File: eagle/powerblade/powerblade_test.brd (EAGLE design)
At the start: 123 x 88 mm, 107 parts, among them J1 JTAG_14PIN_IDC-NL, J21 AC_INFILM, Q1 2N7002, U1 TPS62122, U2 TR1000, U3 MSP430FR5738, U4 LTC5800, U5 MAX9910, U6 MAX9910, X1 ABM8G, X2 ABS07, Y1 UREACH_XTEND, Y2 ANT-916

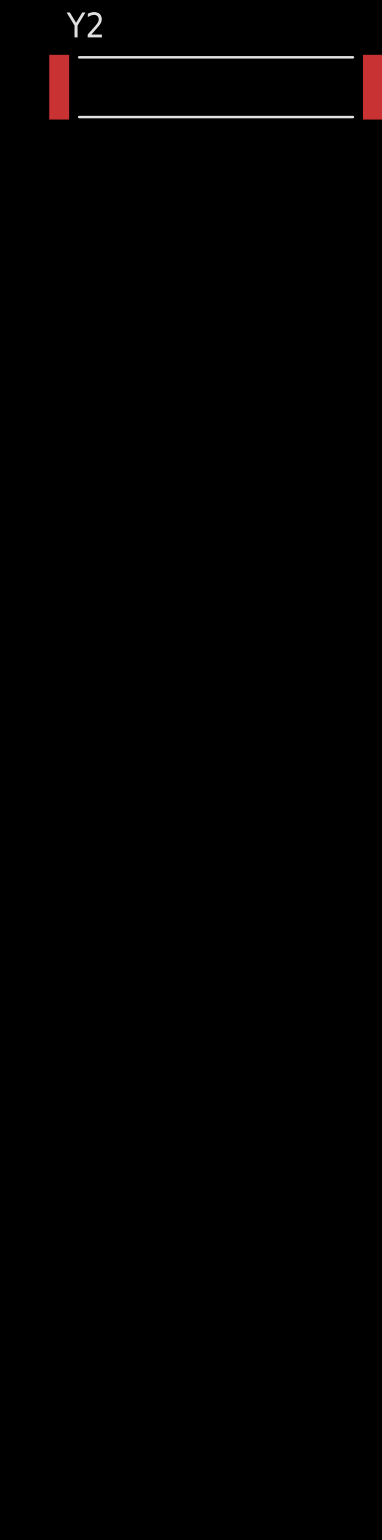
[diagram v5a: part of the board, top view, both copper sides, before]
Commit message: finished final amplifier design including high pass filter and pots for adjusting
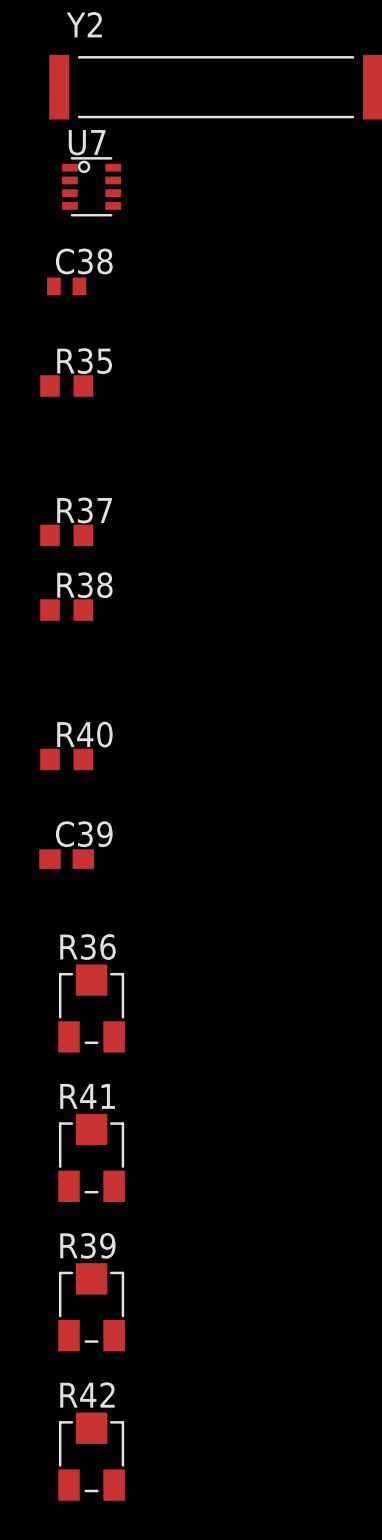
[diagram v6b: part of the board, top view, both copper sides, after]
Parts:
- added C38: 0.1uF, rcl:C0402
- added C39: 1.5uF, rcl:C0603
- added R35: 2k 1%, rcl:R0603
- added R36: 20, powerfilm:3313_POT
- added R37: 90k 1%, rcl:R0603
- added R38: 3.1k 1%, rcl:R0603
- added R39, R41: 10k, powerfilm:3313_POT
- added R40: 100k 1%, rcl:R0603
- added R42: 50k, powerfilm:3313_POT
- added U7: OPA2369, powerfilm:SOT-23-8
- R17: value 1M 1% -> 20k 1%
- R18: value 50 1% -> 2.49 1%
- R20, R21: value 1k 1% -> 10k 1%
- RF: value 1k 1% -> 1.5k 1%
- RI1, RI2: value 120k 1% -> 220k 1%
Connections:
- new net LTC_RCTS: U4.P67
- new net LTC_RRTS: U4.P66
- new net LTC_RX: U4.P68
- new net LTC_TCTS: U4.P70
- new net LTC_TRTS: U4.P69
- new net LTC_TX: U4.P71
- new net N$64: C39.1, R17.2, U5.P4
- new net N$65: R18.2, R36.PW
- new net N$66: R37.1, R41.P2, U7.P6
- new net N$67: C39.2, R42.PW, U7.P5
- new net N$68: R35.1, U7.P1, U7.P2
- new net N$69: R38.2, R41.PW
- new net N$70: R39.P2, R40.1, U7.P3
- new net N$71: R35.2, R42.P2
- net +3V3: now also C38.1, R40.2, U7.P8
- net GND: now also C38.2, R38.1, R39.PW, U7.P4
- net I_SENSE: now also R37.2, U7.P7; no longer R17.2, U5.P4
- net N$39: now also R36.P2; no longer R18.2

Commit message: added power gating or turnoff ability to tr1000, ltc5800, and power metering and defaulted to off
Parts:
- removed Q1: 2N7002, nav:SC-70-3
- removed R10: 10k, rcl:R0402
- removed R11: 47k, rcl:R0603
- removed TP1: TP_STD, skyspecs:TP
- added Q2: 2N7002, nav:SC-70-3
- added R43: 0, rcl:R0603
- added R44, R49: 47k, rcl:R0603
- added R45: 12k, rcl:R0603
- added R46, R47, R48: 33k, rcl:R0603
- added TP2, TP5, TP6, TP7, TP8: TP_STD, skyspecs:TP
- R13: value 10 -> 1 1%
- R15: value 1M 0.1% -> NP
- R16: value 15 0.1% -> 0
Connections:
- removed net N$16: Q1.P3, R10.1, U1.P4
- removed net N$61: R34.1, U3.P14
- removed net PS_!EN!: Q1.P1, R11.1, TP1.P$1
- new net DGND: C27.2, C28.2, C38.2, Q2.P3, R16.1, R18.1, R21.1, R38.1, R39.PW, RI2.1, U5.P2, U6.P2, U7.P4
- new net LTC_SLEEP: R44.2, U3.P15, U4.P35
- new net LTC_TIME: R45.1, U4.P72
- new net METER_EN: Q2.P1, R49.2, U3.P17
- new net N$72: TP7.P$1, U4.P23
- new net N$73: TP6.P$1, U4.P24
- new net N$74: TP5.P$1, U4.P25
- new net N$75: TP2.P$1, U4.P26
- new net N$76: R43.1, U4.P1
- net +3V3: now also R45.2
- net GND: now also Q2.P2, R43.2, R44.1, R46.1, R47.1, R48.1, R49.1; no longer C27.2, C28.2, C38.2, Q1.P2, R11.2, R16.1, R18.1, R21.1, R38.1, R39.PW, RI2.1, U5.P2, U6.P2, U7.P4
- net I_SENSE: now also U3.P6, U4.P17
- net LTC_RRTS: now also R46.2
- net LTC_RX: now also R33.1, R47.2, U3.P13
- net LTC_TCTS: now also R48.2
- net LTC_TX: now also R34.1, U3.P14
- net N$60: now also TP8.P$1, U4.P54; no longer R33.1, U3.P13
- net TCK: no longer U4.P26
- net TDI: no longer U4.P23
- net TDO: no longer U4.P24
- net TMS: no longer U4.P25
- net VCC: now also U1.P4; no longer R10.2
- net V_SENSE: now also U3.P5, U4.P15
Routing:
- net N$16: track 8.33 -> 0.00 mm, vias 2 -> 0
- net VCC: track 13.9 -> 20.7 mm, vias 0 -> 2
- net PS_!EN!: track 4.81 -> 0.00 mm

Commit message: finished layout incl antennas
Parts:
- removed C34: NP, rcl:C0603
- removed C8: 0.1uF, rcl:C0402
- removed R12, R25: NP, rcl:R0603
- removed R23, R24, R27: 0, rcl:R0603
- removed RS-, VS+, VS-: TP_STD, skyspecs:TP
- added ACSLOT: AC_NODIM, powerfilm:AC3_NODIM
- added L7: 100nH, rcl:L0603
- added LED1: (no value), SparkFun-LED:LED-0603
- added Q1: 2SK1829, powerfilm:SC-70-3
- added R10: 120, rcl:R0603
- added TP1, TP9, TPGND1, TPGND2: TP_MULT, skyspecs:TP_MULT
- added TP10, TP11, TP12, TP13: TP_STD, skyspecs:TP
- C10, C39, C4: device rcl:C0603 -> rcl:C0402
- C2: value 15nF -> NP; device rcl:C0603 -> rcl:C2220K
- C29, C30, C31: device rcl:C0201 -> rcl:C0402
- C32: value NP -> 33uF
- C33: value NP -> 15nF
- C7: device rcl:C0402 -> rcl:C0603
- CS+, CS-, HVS, RS+, TP3, TP4: value TP_STD -> TP_MULT; device skyspecs:TP -> skyspecs:TP_MULT
- J21: value AC_INFILM -> AC_INSW; device powerfilm:AC3_FILM -> powerfilm:AC_DC21
- L4: device rcl:L0201 -> rcl:L0402
- Q2: value 2N7002 -> 2SK1829; device nav:SC-70-3 -> powerfilm:SC-70-3
- R14, R15, R16, R17, R18, R20, R21, R35, R37, R38, R40, R43, R44, R45, R46, R47, R48, R7, R9, RF, RI1, RI2: device rcl:R0603 -> rcl:R0402
- TP2, TP5, TP6, TP7: value TP_STD -> TP_SMD; device skyspecs:TP -> skyspecs:TP_SMD
- moved R48 531.2 mm to (104.9, 67.2), flipped to the bottom
- moved Q2 531.1 mm to (32.9, 72.4), flipped to the bottom, turned to 180 degrees
- moved TP8 530.6 mm to (84.5, 66.0), flipped to the bottom
- moved R47 527.6 mm to (103.2, 67.8), flipped to the bottom, turned to 270 degrees
- moved R46 523.2 mm to (100.5, 67.8), flipped to the bottom
- moved R45 519.3 mm to (107.8, 66.5), flipped to the bottom, turned to 180 degrees
- moved R49 516.3 mm to (54.6, 49.5), flipped to the bottom
- moved R43 512.0 mm to (113.2, 67.2), flipped to the bottom, turned to 180 degrees
- moved R44 496.2 mm to (91.8, 52.4), flipped to the bottom, turned to 90 degrees
- moved TP7 487.4 mm to (102.1, 48.7), flipped to the bottom
- moved R42 484.4 mm to (63.5, 78.6), turned to 180 degrees
- moved TP6 482.1 mm to (100.6, 48.7), flipped to the bottom
- moved TP5 476.8 mm to (99.2, 48.7), flipped to the bottom
- moved R39 475.2 mm to (55.6, 78.6), turned to 180 degrees
- moved TP2 471.5 mm to (97.8, 48.7), flipped to the bottom
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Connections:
- removed net N$1: C1.2, HVS.P$1, R1.2, R8.1
- removed net N$56: R24.2, R25.2, R26.1, U2.P11
- removed net N$58: R25.1, U2.P12
- removed net N$59: C33.1, U2.P4
- new net LED_EN: Q2.P1, U3.P16
- new net N$16: L7.2, U2.P2
- net +3V3: now also L7.1, R10.2, U2.P3; no longer R12.1, R23.2, U2.P2, VS+.P$1
- net DGND: now also Q1.P3; no longer Q2.P3
- net GND: now also Q1.P2, TPGND1.P$1, TPGND2.P$1; no longer C33.2, C34.2, C8.2, RS-.P$1, VS-.P$1
- net LTC_RX: now also TP13.P$1
- net LTC_TX: now also TP12.P$1
- net METER_EN: now also Q1.P1; no longer Q2.P1
- net N$12: now also C33.2; no longer R27.1
- net N$4: now also C2.1
- net N$49: now also LED1.A, R10.1; no longer C34.1, R23.1, U2.P3
- net N$50: no longer R12.2
- net N$54: now also LED1.C, Q2.P3; no longer C2.2, C32.1, R27.2
- net N$55: now also C33.1; no longer C2.1
- net N$57: now also R26.1, U2.P11; no longer R24.1
- net N$6: now also J21.L; no longer J21.P
- net N$64: now also TP1.P$1
- net N$67: now also TP9.P$1
- net RXDATA: now also TP11.P$1
- net TXMOD: now also TP10.P$1
- net VCC: now also C32.1; no longer C8.1
- net VTEST: now also C1.2, C2.2, HVS.P$1, R1.2, R8.1
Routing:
- net N$11: track 62.4 -> 1.12 mm, vias 3 -> 1
- net +3V3: track 50.5 -> 0.00 mm, vias 2 -> 0
- net VCC: track 20.7 -> 0.00 mm, vias 2 -> 0
- net N$6: track 19.3 -> 0.00 mm, vias 2 -> 1
- net TMS: track 19.2 -> 0.00 mm, vias 2 -> 0
- net TCK: track 17.4 -> 0.00 mm, vias 2 -> 0
- net TDI: track 17.4 -> 0.00 mm, vias 2 -> 0
- net TEST: track 15.3 -> 0.00 mm, vias 2 -> 0
- net GND: track 15.2 -> 0.00 mm, vias 4 -> 2
- net RST: track 13.4 -> 0.00 mm
- net TDO: track 12.3 -> 0.00 mm
- net N$4: track 10.0 -> 0.00 mm
- net N$1: track 9.14 -> 0.00 mm
- net N$2: track 7.38 -> 0.00 mm
- net N$48: track 0.00 -> 5.66 mm
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- added copper zone on layer 16, net N$11
- added copper zone on layer 16, net N$9
- added copper zone on layer 16, net VCC
- removed copper zone on layer 1, net +3V3
- removed copper zone on layer 1, net N$11
- removed copper zone on layer 1, net N$13
- removed copper zone on layer 1, net N$3
- removed copper zone on layer 1, net N$9
- removed copper zone on layer 1, net VCC
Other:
- outline, holes or cut-outs redrawn
- board text removed: "1.22.15"
- board text removed: "CS+"
- board text removed: "EN"
- board text removed: "HVS"
- board text removed: "RS+"
- board text removed: "S.DeBruin"
- board text removed: "S.Test v2"
- board text removed: "VS+"
